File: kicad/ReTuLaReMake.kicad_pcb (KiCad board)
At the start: 2 copper layers, 54 x 26 mm, 23 parts, among them J1 40 Pin DIP Header, U1 ATF1508AS-10AU100

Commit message: KiCAD: Move PA0
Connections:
- U1 pad 41: unconnected-(U1-Pad41) -> /PA0
- U1 pad 49: /PA0 -> unconnected-(U1-Pad49)
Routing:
- net GND: track 91.1 -> 93.5 mm
- net /PA0: track 10.2 -> 12.1 mm
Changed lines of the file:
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@@
   (net 67 "unconnected-(U1-Pad55)")
   (net 68 "unconnected-(U1-Pad53)")
-  (net 69 "unconnected-(U1-Pad41)")
+  (net 69 "unconnected-(U1-Pad49)")
   (net 70 "unconnected-(U1-Pad40)")
   (net 71 "unconnected-(U1-Pad36)")
@@
       (net 70 "unconnected-(U1-Pad40)") (pinfunction "I/O_30") (pintype "passive+no_connect"))
     (pad "41" smd roundrect (at 1.5 7.6625 270) (size 0.3 1.475) (layers "F.Cu" "F.Paste" "F.Mask") (roundrect_rratio 0.25)
-      (net 69 "unconnected-(U1-Pad41)") (pinfunction "I/O/PD2") (pintype "passive+no_connect"))
+      (net 26 "/PA0") (pinfunction "I/O/PD2") (pintype "passive"))
     (pad "42" smd roundrect (at 2 7.6625 270) (size 0.3 1.475) (layers "F.Cu" "F.Paste" "F.Mask") (roundrect_rratio 0.25)
       (net 25 "/PA1") (pinfunction "I/O_31") (pintype "passive"))
@@
       (net 24 "/PA2") (pinfunction "I/O_36") (pintype "passive"))
     (pad "49" smd roundrect (at 5.5 7.6625 270) (size 0.3 1.475) (layers "F.Cu" "F.Paste" "F.Mask") (roundrect_rratio 0.25)
-      (net 26 "/PA0") (pinfunction "I/O_37") (pintype "passive"))
+      (net 69 "unconnected-(U1-Pad49)") (pinfunction "I/O_37") (pintype "passive+no_connect"))
     (pad "50" smd roundrect (at 6 7.6625 270) (size 0.3 1.475) (layers "F.Cu" "F.Paste" "F.Mask") (roundrect_rratio 0.25)
       (net 97 "unconnected-(U1-Pad50)") (pinfunction "I/O_38") (pintype "passive+no_connect"))
@@
   (segment (start 130.048 122.549) (end 130.048 121.92) (width 0.254) (layer "F.Cu") (net 2))
   (segment (start 127 113.88) (end 127 118.872) (width 0.254) (layer "F.Cu") (net 2))
+  (segment (start 123.25 122.622) (end 123.952 121.92) (width 0.254) (layer "F.Cu") (net 2))
   (segment (start 128 112.88) (end 127 113.88) (width 0.254) (layer "F.Cu") (net 2))
-  (segment (start 122 122.63) (end 122.71 121.92) (width 0.254) (layer "F.Cu") (net 2))
   (segment (start 134.6625 120.38) (end 131.588 120.38) (width 0.254) (layer "F.Cu") (net 2))
   (segment (start 133.04 115.88) (end 130.048 118.872) (width 0.254) (layer "F.Cu") (net 2))
+  (segment (start 122.75 124.13) (end 123.25 123.63) (width 0.254) (layer "F.Cu") (net 2))
   (segment (start 131.75 124.251) (end 130.048 122.549) (width 0.254) (layer "F.Cu") (net 2))
   (segment (start 130.048 118.872) (end 130.048 121.92) (width 0.254) (layer "F.Cu") (net 2))
@@
   (segment (start 123.952 121.92) (end 130.048 121.92) (width 0.254) (layer "F.Cu") (net 2))
   (segment (start 127 118.872) (end 130.048 121.92) (width 0.254) (layer "F.Cu") (net 2))
-  (segment (start 121.5 120.63) (end 122.662 120.63) (width 0.254) (layer "F.Cu") (net 2))
   (segment (start 130.575 129.38) (end 129.7 129.38) (width 0.254) (layer "F.Cu") (net 2))
   (segment (start 125 127.0425) (end 125 125.88) (width 0.254) (layer "F.Cu") (net 2))
   (segment (start 125 125.88) (end 124.5 125.38) (width 0.254) (layer "F.Cu") (net 2))
   (segment (start 115.125 117.88) (end 114 117.88) (width 0.254) (layer "F.Cu") (net 2))
+  (segment (start 122.162 120.13) (end 123.952 121.92) (width 0.254) (layer "F.Cu") (net 2))
   (segment (start 120.25 113.38) (end 120.5 113.63) (width 0.254) (layer "F.Cu") (net 2))
-  (segment (start 120.25 119.38) (end 121.5 120.63) (width 0.254) (layer "F.Cu") (net 2))
+  (segment (start 120.25 119.38) (end 121 120.13) (width 0.254) (layer "F.Cu") (net 2))
   (segment (start 132.5 125.88) (end 131.75 125.13) (width 0.254) (layer "F.Cu") (net 2))
+  (segment (start 121 120.13) (end 122.162 120.13) (width 0.254) (layer "F.Cu") (net 2))
+  (segment (start 131.588 120.38) (end 130.048 121.92) (width 0.254) (layer "F.Cu") (net 2))
   (segment (start 119.3375 121.88) (end 120.25 121.88) (width 0.254) (layer "F.Cu") (net 2))
-  (segment (start 131.588 120.38) (end 130.048 121.92) (width 0.254) (layer "F.Cu") (net 2))
   (segment (start 138.875 121.105) (end 138.875 122.38) (width 0.254) (layer "F.Cu") (net 2))
   (segment (start 119.3375 113.38) (end 120.25 113.38) (width 0.254) (layer "F.Cu") (net 2))
   (segment (start 132.5 127.0425) (end 132.5 125.88) (width 0.254) (layer "F.Cu") (net 2))
   (segment (start 138.875 119.105) (end 138.875 117.88) (width 0.254) (layer "F.Cu") (net 2))
-  (segment (start 122.71 121.92) (end 123.952 121.92) (width 0.254) (layer "F.Cu") (net 2))
   (segment (start 131.75 125.13) (end 131.75 124.251) (width 0.254) (layer "F.Cu") (net 2))
+  (segment (start 121.5 124.13) (end 122.75 124.13) (width 0.254) (layer "F.Cu") (net 2))
   (segment (start 128 111.7175) (end 128 112.88) (width 0.254) (layer "F.Cu") (net 2))
   (segment (start 120.5 115.42) (end 123.952 118.872) (width 0.254) (layer "F.Cu") (net 2))
@@
   (segment (start 118.925 129.38) (end 119.8 129.38) (width 0.254) (layer "F.Cu") (net 2))
   (segment (start 122.425 109.38) (end 121.4 109.38) (width 0.254) (layer "F.Cu") (net 2))
+  (segment (start 120.25 121.88) (end 120.75 122.38) (width 0.254) (layer "F.Cu") (net 2))
+  (segment (start 120.75 122.38) (end 120.75 123.38) (width 0.254) (layer "F.Cu") (net 2))
+  (segment (start 120.75 123.38) (end 121.5 124.13) (width 0.254) (layer "F.Cu") (net 2))
+  (segment (start 119.3375 119.38) (end 120.25 119.38) (width 0.254) (layer "F.Cu") (net 2))
   (segment (start 123.952 118.872) (end 130.048 118.872) (width 0.254) (layer "F.Cu") (net 2))
   (segment (start 120.5 113.63) (end 120.5 115.42) (width 0.254) (layer "F.Cu") (net 2))
-  (segment (start 121 122.63) (end 122 122.63) (width 0.254) (layer "F.Cu") (net 2))
   (segment (start 115.125 119.98) (end 114 119.98) (width 0.254) (layer "F.Cu") (net 2))
-  (segment (start 120.25 121.88) (end 121 122.63) (width 0.254) (layer "F.Cu") (net 2))
   (segment (start 124.5 125.38) (end 124.5 122.468) (width 0.254) (layer "F.Cu") (net 2))
-  (segment (start 122.662 120.63) (end 123.952 121.92) (width 0.254) (layer "F.Cu") (net 2))
   (segment (start 124.5 122.468) (end 123.952 121.92) (width 0.254) (layer "F.Cu") (net 2))
   (segment (start 123.952 118.872) (end 123.952 121.92) (width 0.254) (layer "F.Cu") (net 2))
+  (segment (start 123.25 123.63) (end 123.25 122.622) (width 0.254) (layer "F.Cu") (net 2))
   (segment (start 127 121.92) (end 130.048 118.872) (width 0.254) (layer "F.Cu") (net 2))
-  (segment (start 119.3375 119.38) (end 120.25 119.38) (width 0.254) (layer "F.Cu") (net 2))
   (segment (start 148.59 120.225) (end 148.59 118.11) (width 0.254) (layer "F.Cu") (net 2))
   (via (at 148.59 118.11) (size 0.8) (drill 0.4) (layers "F.Cu" "B.Cu") (net 2))
@@
   (segment (start 115.57 125.095) (end 115.57 127) (width 0.254) (layer "B.Cu") (net 25))
   (segment (start 121.5 121.88) (end 118.785 121.88) (width 0.254) (layer "B.Cu") (net 25))
-  (segment (start 120.25 124.88) (end 121.75 123.38) (width 0.254) (layer "F.Cu") (net 26))
-  (segment (start 121.75 123.38) (end 122 123.38) (width 0.254) (layer "F.Cu") (net 26))
-  (segment (start 119.3375 124.88) (end 120.25 124.88) (width 0.254) (layer "F.Cu") (net 26))
+  (segment (start 119.3375 120.88) (end 121.75 120.88) (width 0.254) (layer "F.Cu") (net 26))
+  (segment (start 121.75 120.88) (end 122.25 121.38) (width 0.254) (layer "F.Cu") (net 26))
+  (segment (start 122.25 123.13) (end 122 123.38) (width 0.254) (layer "F.Cu") (net 26))
+  (segment (start 122.25 121.38) (end 122.25 123.13) (width 0.254) (layer "F.Cu") (net 26))
   (via (at 122 123.38) (size 0.8) (drill 0.4) (layers "F.Cu" "B.Cu") (net 26))
   (segment (start 118.11 124.46) (end 118.11 127) (width 0.254) (layer "B.Cu") (net 26))
@@
   (segment (start 132.5 114.935) (end 132.5 111.7175) (width 0.254) (layer "F.Cu") (net 42))
   (via (at 132.5 114.935) (size 0.8) (drill 0.4) (layers "F.Cu" "B.Cu") (net 42))
-  (segment (start 133.35 115.57) (end 133.135 115.57) (width 0.254) (layer "B.Cu") (net 42))
   (segment (start 133.135 115.57) (end 132.5 114.935) (width 0.254) (layer "B.Cu") (net 42))
   (segment (start 130.5 114.935) (end 130.5 111.7175) (width 0.254) (layer "F.Cu") (net 43))
   (via (at 130.5 114.935) (size 0.8) (drill 0.4) (layers "F.Cu" "B.Cu") (net 43))
-  (segment (start 130.81 115.665) (end 130.81 115.245) (width 0.254) (layer "B.Cu") (net 43))
   (segment (start 130.81 115.245) (end 130.5 114.935) (width 0.254) (layer "B.Cu") (net 43))
   (segment (start 128.5 114.935) (end 128.5 111.7175) (width 0.254) (layer "F.Cu") (net 44))

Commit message: KiCAD: Board settings
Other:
- rule pad_to_mask_clearance: 0 -> 0.05

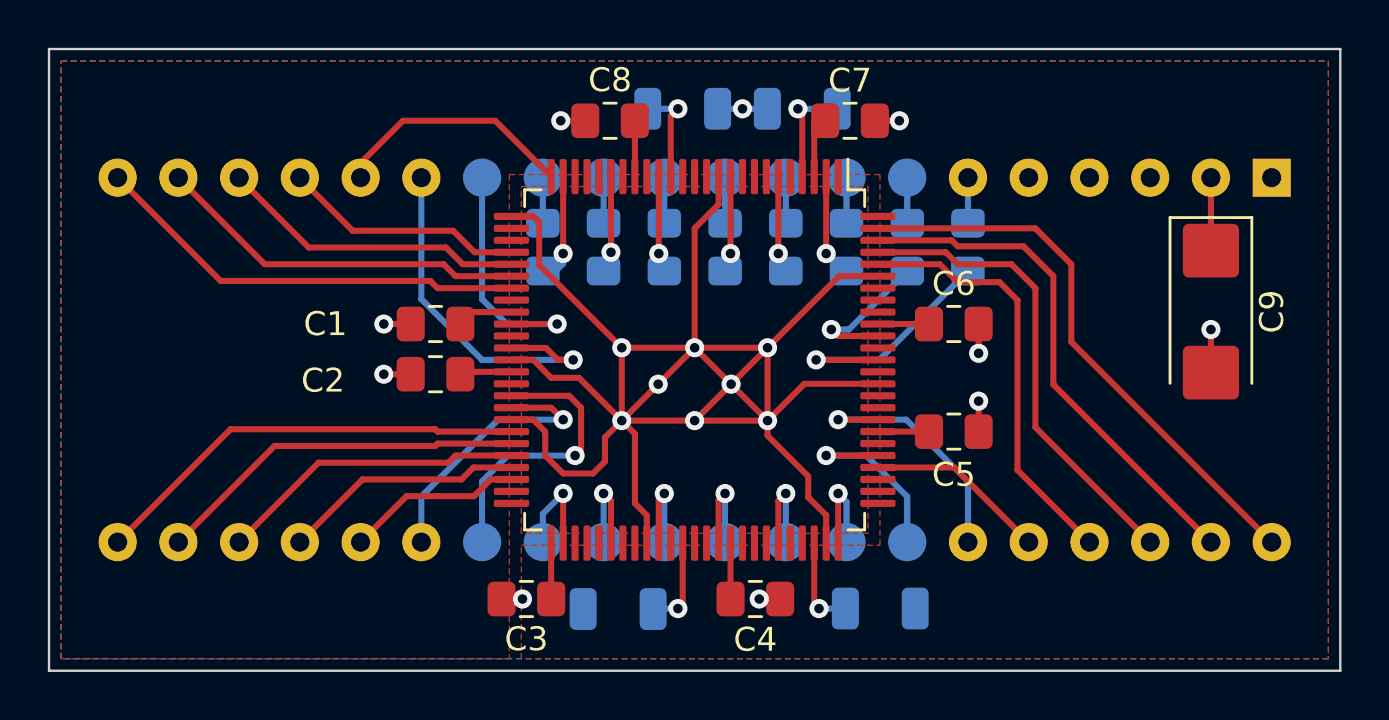
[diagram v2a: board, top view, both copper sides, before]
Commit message: KiCAD: Make VIAs 1.0mm/0.5mm
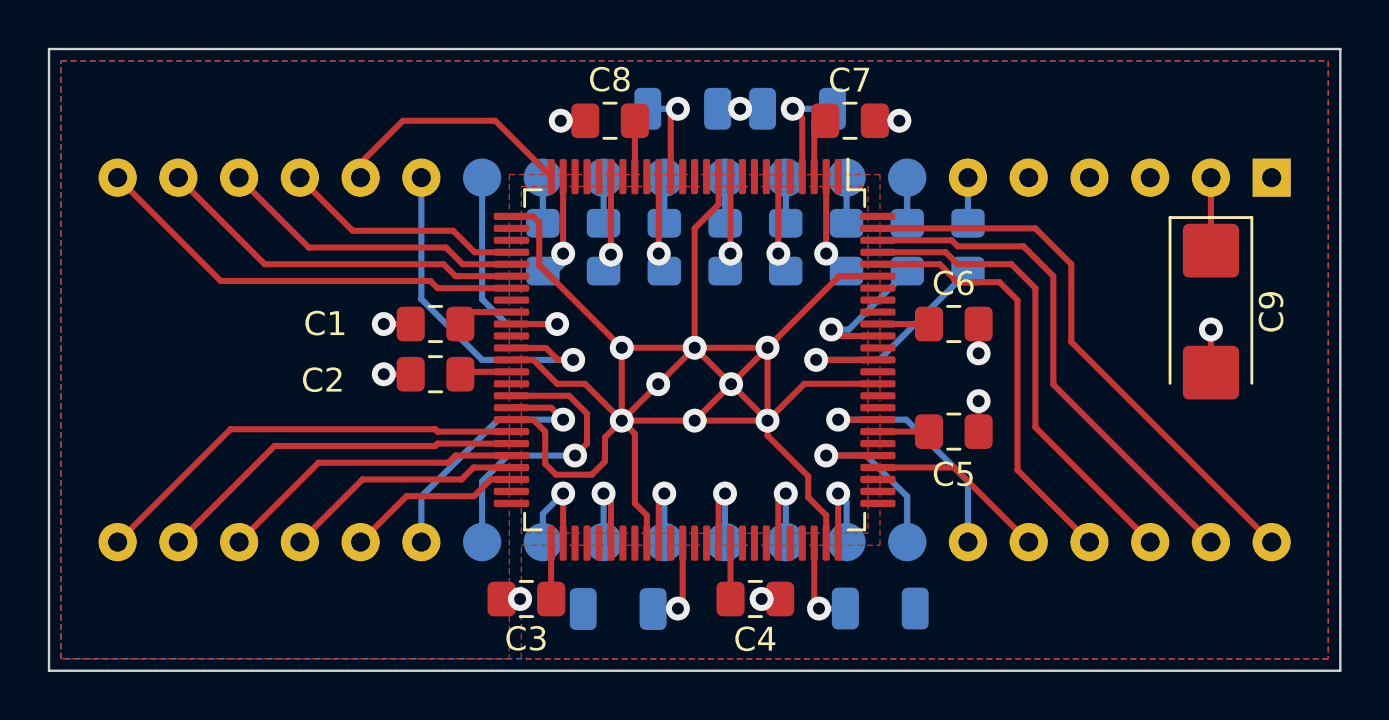
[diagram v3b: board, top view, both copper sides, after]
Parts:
- moved R9 0.20 mm to (131.3, 108.9)

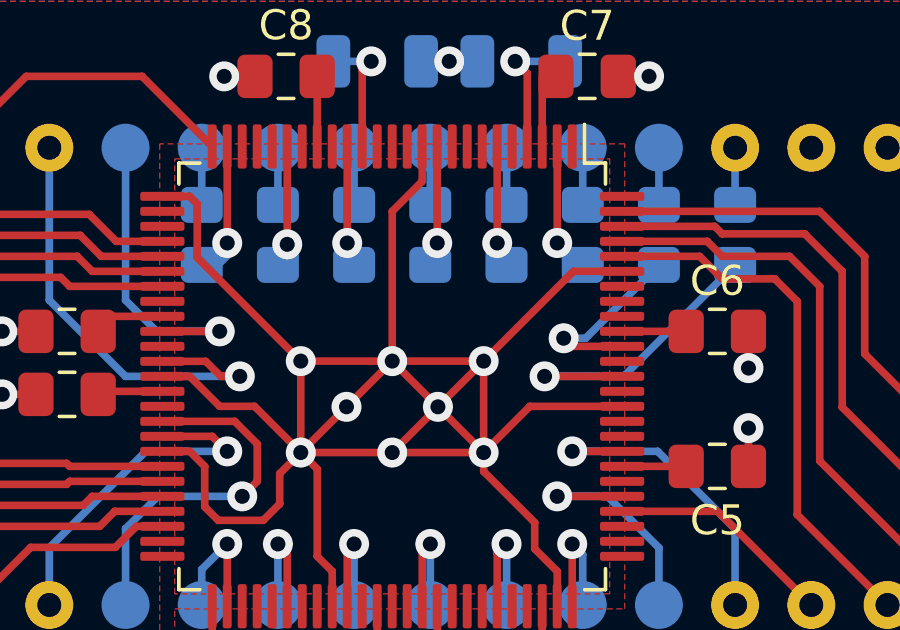
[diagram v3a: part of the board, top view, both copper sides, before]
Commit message: KiCAD: Move HD1/0 to valid pins
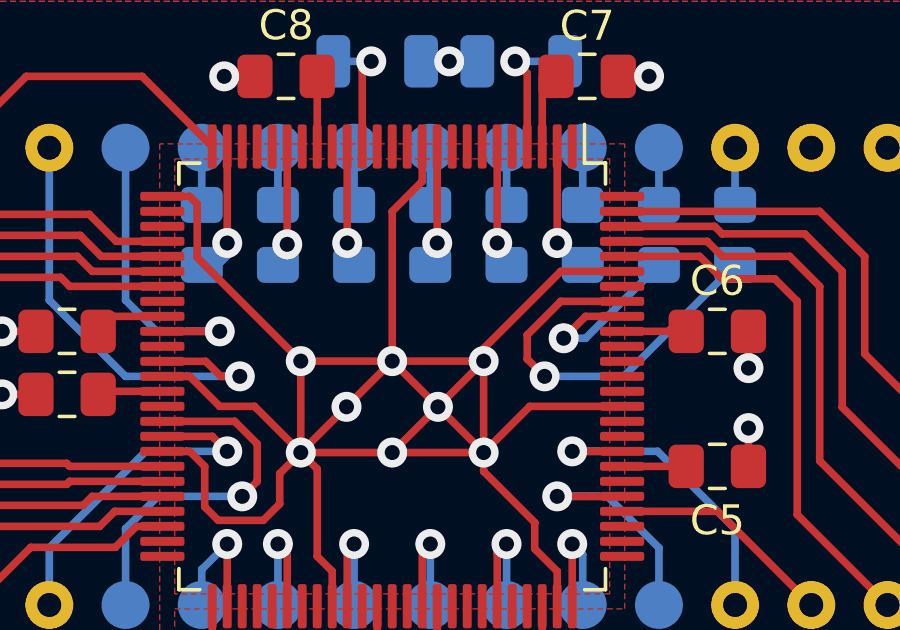
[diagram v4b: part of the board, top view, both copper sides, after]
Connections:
- U1 pad 88: /HD0 -> unconnected-(U1-Pad88)
- U1 pad 90: /HD1 -> unconnected-(U1-Pad90)
- U1 pad 92: unconnected-(U1-Pad92) -> /HD1
- U1 pad 93: unconnected-(U1-Pad93) -> /HD0
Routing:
- net /HD0: track 10.5 -> 13.1 mm
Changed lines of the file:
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@@
     (pad_to_mask_clearance 0.05)
     (solder_mask_min_width 0.1)
-    (grid_origin 127 119.38)
     (pcbplotparams
       (layerselection 0x00010fc_ffffffff)
@@
   (net 52 "unconnected-(U1-Pad100)")
   (net 53 "unconnected-(U1-Pad94)")
-  (net 54 "unconnected-(U1-Pad93)")
-  (net 55 "unconnected-(U1-Pad92)")
+  (net 54 "unconnected-(U1-Pad88)")
+  (net 55 "unconnected-(U1-Pad90)")
   (net 56 "unconnected-(U1-Pad89)")
   (net 57 "unconnected-(U1-Pad87)")
@@
       (net 57 "unconnected-(U1-Pad87)") (pinfunction "INPUT/GCLK1") (pintype "passive+no_connect"))
     (pad "88" smd roundrect (at 0 -7.6625 270) (size 0.3 1.475) (layers "F.Cu" "F.Paste" "F.Mask") (roundrect_rratio 0.25)
-      (net 40 "/HD0") (pinfunction "INPUT/OE1") (pintype "passive"))
+      (net 54 "unconnected-(U1-Pad88)") (pinfunction "INPUT/OE1") (pintype "passive+no_connect"))
     (pad "89" smd roundrect (at -0.5 -7.6625 270) (size 0.3 1.475) (layers "F.Cu" "F.Paste" "F.Mask") (roundrect_rratio 0.25)
       (net 56 "unconnected-(U1-Pad89)") (pinfunction "INPUT/GCLR") (pintype "passive+no_connect"))
     (pad "90" smd roundrect (at -1 -7.6625 270) (size 0.3 1.475) (layers "F.Cu" "F.Paste" "F.Mask") (roundrect_rratio 0.25)
-      (net 41 "/HD1") (pinfunction "INPUT/OE2/GCLK2") (pintype "passive"))
+      (net 55 "unconnected-(U1-Pad90)") (pinfunction "INPUT/OE2/GCLK2") (pintype "passive+no_connect"))
     (pad "91" smd roundrect (at -1.5 -7.6625 270) (size 0.3 1.475) (layers "F.Cu" "F.Paste" "F.Mask") (roundrect_rratio 0.25)
       (net 1 "VCC") (pinfunction "VCCINT_2") (pintype "passive"))
     (pad "92" smd roundrect (at -2 -7.6625 270) (size 0.3 1.475) (layers "F.Cu" "F.Paste" "F.Mask") (roundrect_rratio 0.25)
-      (net 55 "unconnected-(U1-Pad92)") (pinfunction "I/O_66") (pintype "passive+no_connect"))
+      (net 41 "/HD1") (pinfunction "I/O_66") (pintype "passive"))
     (pad "93" smd roundrect (at -2.5 -7.6625 270) (size 0.3 1.475) (layers "F.Cu" "F.Paste" "F.Mask") (roundrect_rratio 0.25)
-      (net 54 "unconnected-(U1-Pad93)") (pinfunction "I/O_67") (pintype "passive+no_connect"))
+      (net 40 "/HD0") (pinfunction "I/O_67") (pintype "passive"))
     (pad "94" smd roundrect (at -3 -7.6625 270) (size 0.3 1.475) (layers "F.Cu" "F.Paste" "F.Mask") (roundrect_rratio 0.25)
       (net 53 "unconnected-(U1-Pad94)") (pinfunction "I/O_68") (pintype "passive+no_connect"))
@@
   (segment (start 129.8375 108.88) (end 128.9 108.88) (width 0.254) (layer "B.Cu") (net 1))
   (segment (start 127.9625 108.88) (end 128.9 108.88) (width 0.254) (layer "B.Cu") (net 1))
+  (segment (start 134.6625 115.88) (end 132.62 115.88) (width 0.254) (layer "F.Cu") (net 2))
   (segment (start 123.25 123.63) (end 123.25 122.622) (width 0.254) (layer "F.Cu") (net 2))
   (segment (start 130.048 122.549) (end 130.048 121.92) (width 0.254) (layer "F.Cu") (net 2))
@@
   (segment (start 134.6625 120.38) (end 131.588 120.38) (width 0.254) (layer "F.Cu") (net 2))
   (segment (start 118.925 129.38) (end 119.7 129.38) (width 0.254) (layer "F.Cu") (net 2))
-  (segment (start 133.04 115.88) (end 130.048 118.872) (width 0.254) (layer "F.Cu") (net 2))
   (segment (start 131.75 124.251) (end 130.048 122.549) (width 0.254) (layer "F.Cu") (net 2))
   (segment (start 130.048 118.872) (end 130.048 121.92) (width 0.254) (layer "F.Cu") (net 2))
-  (segment (start 134.6625 115.88) (end 133.04 115.88) (width 0.254) (layer "F.Cu") (net 2))
   (segment (start 123.952 121.92) (end 130.048 121.92) (width 0.254) (layer "F.Cu") (net 2))
   (segment (start 120.75 122.38) (end 120.75 123.73) (width 0.254) (layer "F.Cu") (net 2))
@@
   (segment (start 134.536 109.38) (end 135.561 109.38) (width 0.254) (layer "F.Cu") (net 2))
   (segment (start 122.425 109.38) (end 121.4 109.38) (width 0.254) (layer "F.Cu") (net 2))
+  (segment (start 132.62 115.88) (end 130.048 118.452) (width 0.254) (layer "F.Cu") (net 2))
   (segment (start 121.2 124.18) (end 122.7 124.18) (width 0.254) (layer "F.Cu") (net 2))
   (segment (start 120.25 119.38) (end 121.25 120.38) (width 0.254) (layer "F.Cu") (net 2))
   (segment (start 123.952 118.872) (end 130.048 118.872) (width 0.254) (layer "F.Cu") (net 2))
+  (segment (start 130.048 118.452) (end 130.048 118.872) (width 0.254) (layer "F.Cu") (net 2))
   (segment (start 120.5 113.63) (end 120.5 115.42) (width 0.254) (layer "F.Cu") (net 2))
   (segment (start 115.125 119.98) (end 114 119.98) (width 0.254) (layer "F.Cu") (net 2))
@@
   (segment (start 141.25 113.88) (end 142.75 115.38) (width 0.254) (layer "F.Cu") (net 39))
   (segment (start 142.75 115.38) (end 142.75 118.63) (width 0.254) (layer "F.Cu") (net 39))
-  (segment (start 134.6625 119.38) (end 132.08 119.38) (width 0.254) (layer "F.Cu") (net 40))
+  (segment (start 131.5 118) (end 131.5 118.8) (width 0.254) (layer "F.Cu") (net 40))
+  (segment (start 134.6625 116.88) (end 132.62 116.88) (width 0.254) (layer "F.Cu") (net 40))
+  (segment (start 131.5 118.8) (end 132.08 119.38) (width 0.254) (layer "F.Cu") (net 40))
+  (segment (start 132.62 116.88) (end 131.5 118) (width 0.254) (layer "F.Cu") (net 40))
   (via (at 132.08 119.38) (size 1) (drill 0.5) (layers "F.Cu" "B.Cu") (net 40))
   (segment (start 134.715 119.38) (end 132.08 119.38) (width 0.254) (layer "B.Cu") (net 40))
   (segment (start 138.43 115.665) (end 134.715 119.38) (width 0.254) (layer "B.Cu") (net 40))
-  (segment (start 132.985 118.38) (end 132.715 118.11) (width 0.254) (layer "F.Cu") (net 41))
-  (segment (start 134.6625 118.38) (end 132.985 118.38) (width 0.254) (layer "F.Cu") (net 41))
+  (segment (start 134.6625 117.38) (end 133.445 117.38) (width 0.254) (layer "F.Cu") (net 41))
+  (segment (start 133.445 117.38) (end 132.715 118.11) (width 0.254) (layer "F.Cu") (net 41))
   (via (at 132.715 118.11) (size 1) (drill 0.5) (layers "F.Cu" "B.Cu") (net 41))
   (segment (start 133.445 118.11) (end 132.715 118.11) (width 0.254) (layer "B.Cu") (net 41))
@@
   (via (at 123.5 114.98) (size 1) (drill 0.5) (layers "F.Cu" "B.Cu") (net 46))
   (segment (start 123.5 114.98) (end 123.19 115.29) (width 0.254) (layer "B.Cu") (net 46))
-  (segment (start 123.19 115.29) (end 123.19 115.665) (width 0.254) (layer "B.Cu") (net 46))
   (segment (start 121.5 114.935) (end 121.5 111.7175) (width 0.254) (layer "F.Cu") (net 47))
   (via (at 121.5 114.935) (size 1) (drill 0.5) (layers "F.Cu" "B.Cu") (net 47))
